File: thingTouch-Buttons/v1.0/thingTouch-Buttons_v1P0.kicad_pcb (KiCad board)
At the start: 2 copper layers, 160 x 48 mm, 57 parts, among them P1 DIRECT_CONN, P2 TOUCH_CONN, U1 TTP224N-BSB

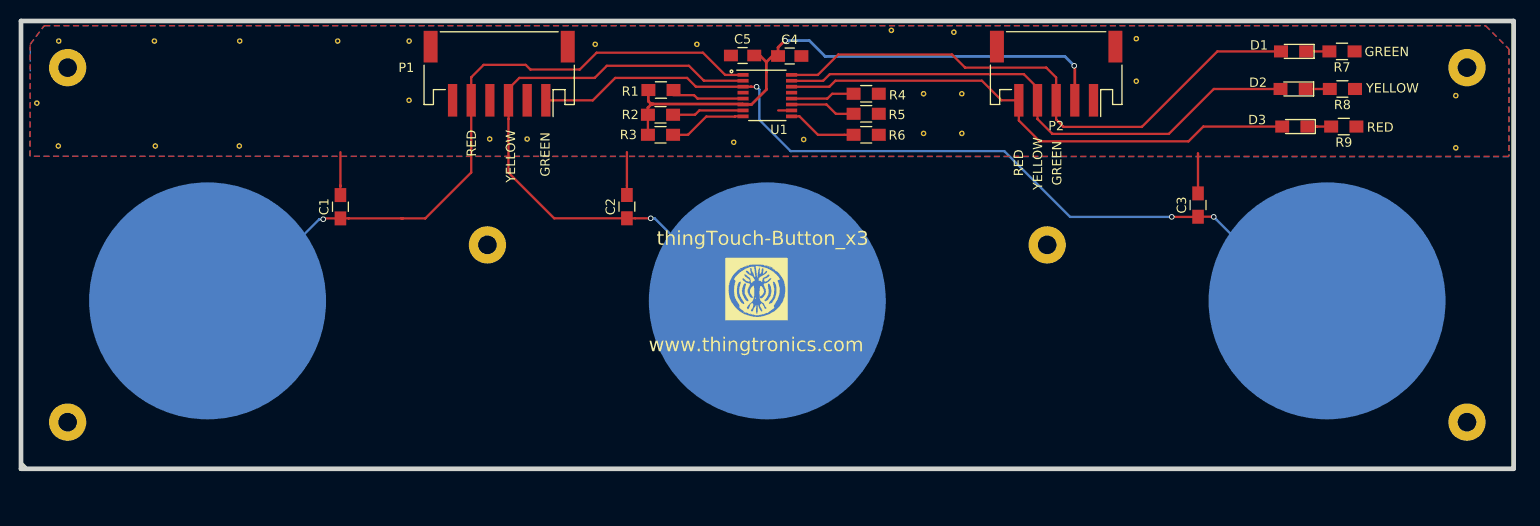
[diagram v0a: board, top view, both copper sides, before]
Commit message: in schematic transistor switching,side leds added right angle connector s added
in schematic transistor switching logic, side leds added ,right angle
connector s added
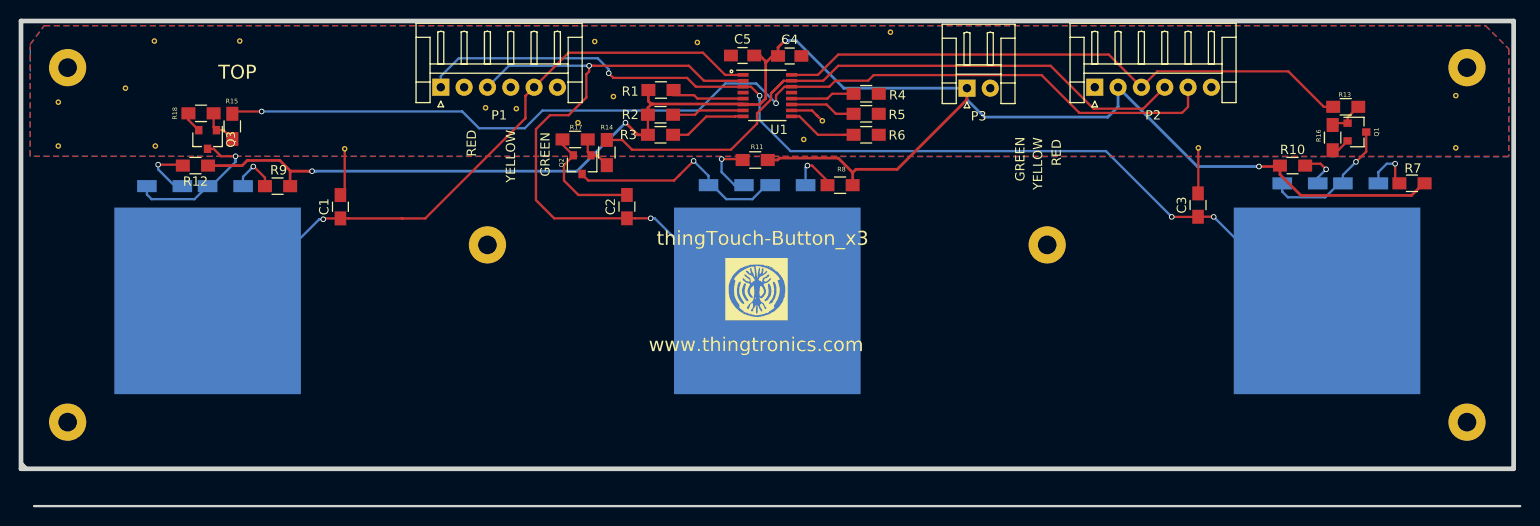
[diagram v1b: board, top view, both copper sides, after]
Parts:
- removed the REF** at (166.8, 87.8)
- removed the REF** at (170.0, 81.2)
- removed the REF** at (104.0, 82.2)
- removed the REF** at (111.6, 82.2)
- removed the REF** at (111.6, 88.5)
- removed the REF** at (189.6, 81.9)
- removed the REF** at (189.6, 86.5)
- removed the REF** at (146.4, 93.0)
- removed the REF** at (166.8, 92.0)
- removed the REF** at (170.8, 92.0)
- removed the REF** at (170.8, 87.8)
- added D4: LED0, SIM_MODULES:LED_0805_Side_led, B.Cu at (207.1, 97.4)
- added D5: LED1, SIM_MODULES:LED_0805_Side_led, B.Cu at (145.6, 97.6)
- added D6: LED2, SIM_MODULES:LED_0805_Side_led, B.Cu at (85.4, 97.7)
- added P3: CONN_01X02, Connectors_JST:JST_EH_S02B-EH_02x2.50mm_Angled, F.Cu at (171.4, 87.2)
- added Q1: MMBT3904, TO_SOT_Packages_SMD:SOT-23, F.Cu at (213.2, 91.9)
- added Q2: MMBT3904, TO_SOT_Packages_SMD:SOT-23, F.Cu at (130.2, 95.4)
- added Q3: MMBT3904, TO_SOT_Packages_SMD:SOT-23, F.Cu at (90.0, 92.7)
- added R10: 1K, Resistors_SMD:R_0805_HandSoldering, F.Cu at (206.3, 95.5)
- added R11: 1K, Resistors_SMD:R_0805_HandSoldering, F.Cu at (148.7, 94.9)
- added R12: 1K, Resistors_SMD:R_0805_HandSoldering, F.Cu at (88.7, 95.5)
- added R13: 4.7K, Resistors_SMD:R_0805_HandSoldering, F.Cu at (212.0, 89.2)
- added R14: 4.7K, Resistors_SMD:R_0805_HandSoldering, F.Cu at (132.8, 94.1)
- added R15: 4.7K, Resistors_SMD:R_0805_HandSoldering, F.Cu at (92.7, 91.3)
- added R16: 47K, Resistors_SMD:R_0805_HandSoldering, F.Cu at (210.6, 92.5)
- added R17: 47K, Resistors_SMD:R_0805_HandSoldering, F.Cu at (129.4, 92.7)
- added R18: 47K, Resistors_SMD:R_0805_HandSoldering, F.Cu at (89.3, 89.9)
- added REF**: VIA_0.6mm, via:VIA_0.6mm, F.Cu at (129.7, 90.9)
- added REF**: VIA_0.6mm, via:VIA_0.6mm, F.Cu at (133.5, 88.1)
- added REF**: VIA_0.6mm, via:VIA_0.6mm, F.Cu at (155.9, 90.7)
- added REF**: VIA_0.6mm, via:VIA_0.6mm, F.Cu at (196.2, 93.6)
- D1, D2, D3: footprint LEDs:LED_0805_HandSoldering -> SIM_MODULES:LED_0805_Side_led; moved to B.Cu
- P1: footprint Connectors_JST:JST_PH_S6B-PH-SM4-TB_06x2.00mm_Angled -> Connectors_JST:JST_EH_S06B-EH_06x2.50mm_Angled
- P2: footprint Connectors_JST:JST_PH_S5B-PH-SM4-TB_05x2.00mm_Angled -> Connectors_JST:JST_EH_S06B-EH_06x2.50mm_Angled
- moved D3 114.8 mm to (91.9, 97.7), turned to 0 degrees
- moved R9 114.5 mm to (97.5, 97.7)
- moved D2 55.1 mm to (152.2, 97.6), turned to 0 degrees
- moved R8 54.8 mm to (157.8, 97.6)
- moved R7 16.0 mm to (219.1, 97.4)
- moved D1 15.9 mm to (213.6, 97.4), turned to 0 degrees
- moved REF** 15.0 mm to (18.6, 80.8)
- moved REF** 11.3 mm to (104.7, 93.7)
- moved REF** 8.75 mm to (81.2, 87.2)
- moved P1 6.43 mm to (115.0, 87.1), turned to 0 degrees
- moved P2 4.39 mm to (185.1, 87.1), turned to 0 degrees
- moved REF** 3.45 mm to (123.1, 89.4)
- moved REF** 3.38 mm to (119.8, 89.3)
- moved REF** 2.30 mm to (74.0, 88.7)
- moved REF** 0.30 mm to (131.5, 82.2)
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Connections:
- P2 pad 3: Net-(D1-Pad2) -> Net-(P2-Pad3)
- P2 pad 4: Net-(D2-Pad2) -> Net-(P2-Pad4)
- P2 pad 5: Net-(D3-Pad2) -> Net-(P2-Pad5)
- R7 pad 1: GND -> VDD
- R7 pad 2: Net-(D1-Pad1) -> Net-(D1-Pad2)
- R8 pad 1: GND -> VDD
- R8 pad 2: Net-(D2-Pad1) -> Net-(D2-Pad2)
- R9 pad 1: GND -> VDD
- R9 pad 2: Net-(D3-Pad1) -> Net-(D3-Pad2)
- U1 pad 14: Net-(D3-Pad2) -> Net-(P2-Pad5)
- U1 pad 15: Net-(D2-Pad2) -> Net-(P2-Pad4)
- U1 pad 16: Net-(D1-Pad2) -> Net-(P2-Pad3)
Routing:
- net VDD: track 62.5 -> 188.5 mm, vias 2 -> 4
- net Net-(P2-Pad5): track 0.00 -> 112.0 mm, vias 0 -> 2
- net Net-(P2-Pad4): track 0.00 -> 69.7 mm
- net Net-(P2-Pad3): track 0.00 -> 62.7 mm
- net Net-(D1-Pad2): track 62.6 -> 5.66 mm, vias 0 -> 1
- net Net-(D2-Pad2): track 59.3 -> 5.47 mm, vias 0 -> 1
- net Net-(D3-Pad2): track 57.5 -> 5.20 mm, vias 0 -> 1
- net Net-(D2-Pad1): track 2.58 -> 24.2 mm, vias 0 -> 1
- net GND: track 14.9 -> 31.5 mm
- net Net-(D3-Pad1): track 2.55 -> 16.2 mm, vias 0 -> 1
- net Net-(C3-Pad1): track 96.6 -> 109.6 mm, vias 3 -> 4
- net Net-(D1-Pad1): track 2.49 -> 14.8 mm, vias 0 -> 1
- net Net-(C2-Pad1): track 69.3 -> 76.2 mm, vias 1 -> 2
- net Net-(D5-Pad2): track 0.00 -> 6.67 mm, vias 0 -> 1
- net Net-(D6-Pad2): track 0.00 -> 6.54 mm, vias 0 -> 1
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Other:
- board size 160 x 48 mm -> 160.7 x 52 mm
- board text added: "BOTTOM"
- board text added: "TOP"

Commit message: verified the layout
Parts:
- P3: value CONN_01X02 -> POWER_CONN
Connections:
- R13 pad 1: Net-(P2-Pad3) -> Net-(P2-Pad5)
- R15 pad 1: Net-(P2-Pad5) -> Net-(P2-Pad3)
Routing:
- net Net-(P2-Pad5): track 112.0 -> 67.2 mm, vias 2 -> 1
- net Net-(P2-Pad3): track 62.7 -> 102.5 mm, vias 0 -> 2
- net Net-(P2-Pad4): track 69.7 -> 70.4 mm
